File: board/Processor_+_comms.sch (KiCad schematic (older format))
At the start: 39 parts, among them U11 ATXMEGA256A3U-MH, U12 NTS0104, U14 TC1015-3.3VCT713

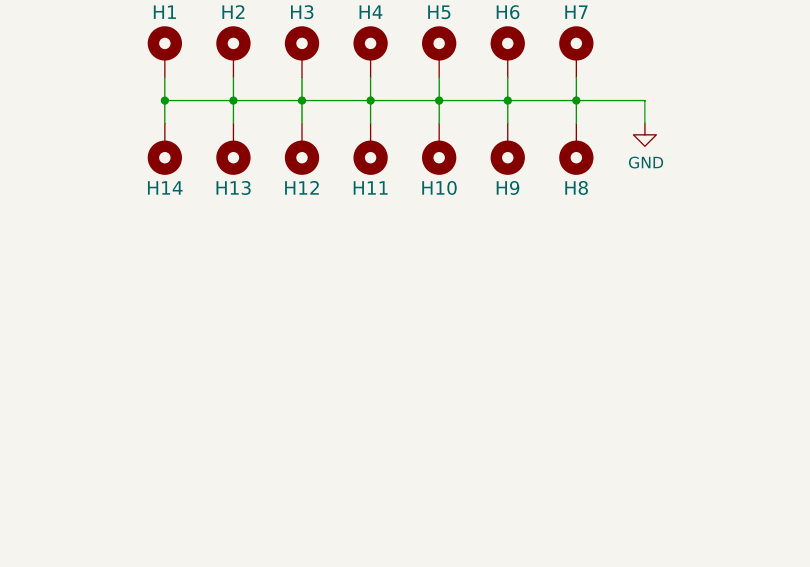
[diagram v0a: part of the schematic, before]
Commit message: Added two fiducial marks and fixed a couple more footprints
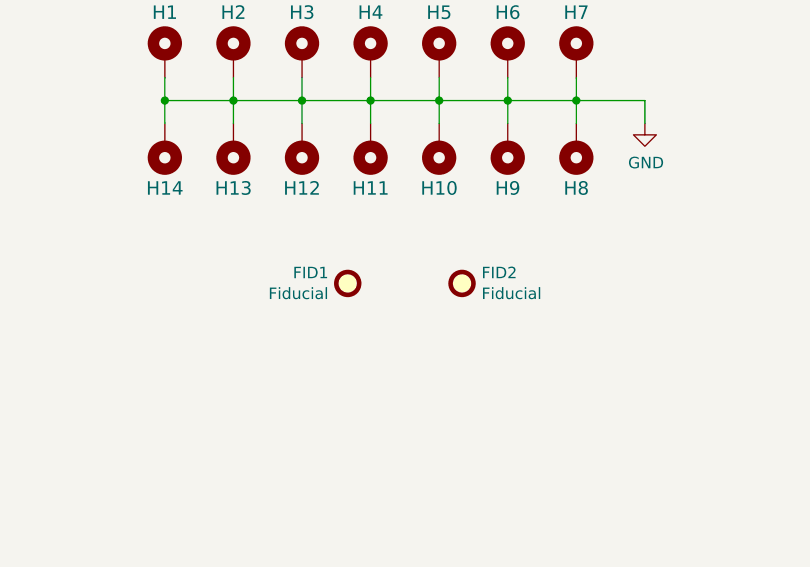
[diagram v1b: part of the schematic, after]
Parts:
- added FID1, FID2: Fiducial, Fiducial:Fiducial_1mm_Mask2mm, symbol Mechanical:Fiducial
- OSC1: footprint MXKeyboard_RGB:7M -> rhais_osc:SMD3225
- U12: footprint MXKeyboard_RGB:DHVQFN-14 -> rhais_package-qfn:DHVQFN-14-1EP_2.5x3mm_P0.5mm_EP1x1.5mm
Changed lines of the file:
@@
 F 0 "U12" H 13200 5980 59  0000 R TNN
 F 1 "NTS0104" H 12400 5980 59  0000 L TNN
-F 2 "MXKeyboard_RGB:DHVQFN-14" H 12800 6500 50  0001 C CNN
+F 2 "rhais_package-qfn:DHVQFN-14-1EP_2.5x3mm_P0.5mm_EP1x1.5mm" H 12800 6500 50  0001 C CNN
 F 3 "" H 12800 6500 50  0001 C CNN
 F 4 "NXP" H 12800 6500 59  0001 L BNN "MFR"
@@
 F 0 "OSC1" H 10000 1780 85  0000 L TNN
 F 1 "16MHz" H 9500 2620 85  0000 L BNN
-F 2 "MXKeyboard_RGB:7M" H 9900 2200 50  0001 C CNN
+F 2 "rhais_osc:SMD3225" H 9900 2200 50  0001 C CNN
 F 3 "" H 9900 2200 50  0001 C CNN
 F 4 "Multicomp" H 9900 2200 85  0001 L BNN "ALT_MFR"
@@
 $EndComp
 NoConn ~ 3900 2300
+$Comp
+L Mechanical:Fiducial FID1
+U 1 1 603C2F69
+P 13000 3000
+F 0 "FID1" H 12916 2954 50  0000 R CNN
+F 1 "Fiducial" H 12916 3045 50  0000 R CNN
+F 2 "Fiducial:Fiducial_1mm_Mask2mm" H 13000 3000 50  0001 C CNN
+F 3 "~" H 13000 3000 50  0001 C CNN
+	1    13000 3000
+	1    0    0    1
+$EndComp
+$Comp
+L Mechanical:Fiducial FID2
+U 1 1 603C34BD
+P 13500 3000
+F 0 "FID2" H 13585 3046 50  0000 L CNN
+F 1 "Fiducial" H 13585 2955 50  0000 L CNN
+F 2 "Fiducial:Fiducial_1mm_Mask2mm" H 13500 3000 50  0001 C CNN
+F 3 "~" H 13500 3000 50  0001 C CNN
+	1    13500 3000
+	1    0    0    -1
+$EndComp
 Wire Bus Line
 	4350 4400 4350 4800

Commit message: Renamed MXKeyboard_RGB => MXKeyboard and cleaned up the last of the old Eagle files we aren't using now
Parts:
- OSC1: symbol MXKeyboard_RGB-eagle-import:CXO-7M -> MXKeyboard-eagle-import:CXO-7M
- PS/2: footprint MXKeyboard_RGB:TM_0508_A_6 -> MXKeyboard:TM_0508_A_6; symbol MXKeyboard_RGB-eagle-import:PS_2 -> MXKeyboard-eagle-import:PS_2
- U11: symbol MXKeyboard_RGB-eagle-import:ATXMEGA256A3U-MH -> MXKeyboard-eagle-import:ATXMEGA256A3U-MH
- U12: symbol MXKeyboard_RGB-eagle-import:NTS0104 -> MXKeyboard-eagle-import:NTS0104
- U14: symbol MXKeyboard_RGB-eagle-import:TC1015-3.3VCT713 -> MXKeyboard-eagle-import:TC1015-3.3VCT713
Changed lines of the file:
@@
 $EndComp
 $Comp
-L MXKeyboard_RGB-eagle-import:PS_2 PS/2
+L MXKeyboard-eagle-import:PS_2 PS/2
 U 1 1 554878EE
 P 14300 6300
@@
 F 0 "PS/2" H 14300 6300 50  0001 C CNN
 F 1 "PS_2" H 14300 6300 50  0001 C CNN
-F 2 "MXKeyboard_RGB:TM_0508_A_6" H 14300 6300 50  0001 C CNN
+F 2 "MXKeyboard:TM_0508_A_6" H 14300 6300 50  0001 C CNN
 F 3 "https://downloads.lumberg.com/datenblaetter/en/tm0508a.pdf" H 14300 6300 50  0001 C CNN
 F 4 "https://uk.farnell.com/lumberg/tm-0508-a-6/socket-mini-din-chassis-6-way/dp/1200113" H 14300 6300 50  0001 C CNN "URL_FARNELL"
@@
 $EndComp
 $Comp
-L MXKeyboard_RGB-eagle-import:NTS0104 U12
+L MXKeyboard-eagle-import:NTS0104 U12
 U 1 1 A9F22F29
 P 12800 6500
@@
 $EndComp
 $Comp
-L MXKeyboard_RGB-eagle-import:TC1015-3.3VCT713 U14
+L MXKeyboard-eagle-import:TC1015-3.3VCT713 U14
 U 1 1 9D30ECAF
 P 7700 2200
@@
 $EndComp
 $Comp
-L MXKeyboard_RGB-eagle-import:CXO-7M OSC1
+L MXKeyboard-eagle-import:CXO-7M OSC1
 U 1 1 01133300
 P 9900 2200
@@
 $EndComp
 $Comp
-L MXKeyboard_RGB-eagle-import:ATXMEGA256A3U-MH U11
+L MXKeyboard-eagle-import:ATXMEGA256A3U-MH U11
 U 1 1 43CCD586
 P 5700 5800

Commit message: Cleaned up the BOM and added all the missing BOM information I could find
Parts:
- C1, C2, C3, C4, C5, C6, C7, C8, C9: URL_FARNELL (none) -> https://uk.farnell.com/multicomp/mc0603b104j250ct/cap-0-1-f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
- C11, C13: MPN MC0603X105K100CT -> MC0603B105K160CT; OC_FARNELL 1759399 -> 2320814; URL_FARNELL https://uk.farnell.com/multicomp/mc0603x105k100ct/cap-1-f-1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 -> https://uk.farnell.com/multicomp/mc0603b105k160ct/cap-1-f-1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
- JP1: MFR (none) -> Amphenol ICC; MPN (none) -> 20021121-00010C4LF; OC_FARNELL (none) -> 1865279; URL_FARNELL (none) -> https://uk.farnell.com/amphenol-icc-fci/20021121-00010c4lf/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
- OSC1: ALT_MFR Multicomp -> (none); ALT_MPN MCSJK-3N-16.00-3.3-25-B -> (none); ALT_OC_FARNELL 2854286 -> (none); ALT_URL https://uk.farnell.com/multicomp/mcsjk-3n-16-00-3-3-25-b/os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 -> (none); MFR IQD -> Multicomp; MPN LFSPXO025494 -> MCSJK-3N-16.00-3.3-25-B; OC_FARNELL 2449455 -> 2854286; URL_FARNELL http://uk.farnell.com/iqd-frequency-products/lfspxo025494/o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 -> https://uk.farnell.com/multicomp/mcsjk-3n-16-00-3-3-25-b/os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
- R17, R19: MFR Vishay -> Multicomp; MPN CRCW08051M00FKEA -> MCWR06X1004FTL; OC_FARNELL 1652946 -> 2447285; URL_FARNELL https://uk.farnell.com/vishay/crcw08051m00fkea/res-1m-1-0-1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 -> https://uk.farnell.com/multicomp/mcwr06x1004ftl/res-1m-1-0-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
- R18, R38: MPN MC0063W0603110K -> MCWR06X1002FTL; OC_FARNELL 2130939 -> 2446547; URL_FARNELL (none) -> https://uk.farnell.com/multicomp/mcwr06x1002ftl/res-10k-1-0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
- R37: MFR (none) -> Multicomp; MPN (none) -> MCWR06X1003FTL; OC_FARNELL (none) -> 2447226; URL_FARNELL (none) -> https://uk.farnell.com/multicomp/mcwr06x1003ftl/res-100k-1-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
- U11: MFR (none) -> Atmel; MPN (none) -> ATXMEGA256A3U-MH; OC_FARNELL (none) -> 2066308; URL_FARNELL (none) -> https://uk.farnell.com/microchip/atxmega256a3u-mh/mcu-8bit-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
- U14: MFR (none) -> Microchip; MPN (none) -> TC1015-3.3VCT713; OC_FARNELL (none) -> 1331505; URL_FARNELL (none) -> https://uk.farnell.com/microchip/tc1015-3-3vct713/ic-v-reg-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
- USB: MFR (none) -> Amphenol ICC; MPN (none) -> 10103593-0001LF; OC_FARNELL (none) -> 2293751; URL_FARNELL (none) -> https://uk.farnell.com/amphenol-icc-fci/10103593-0001lf/mic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

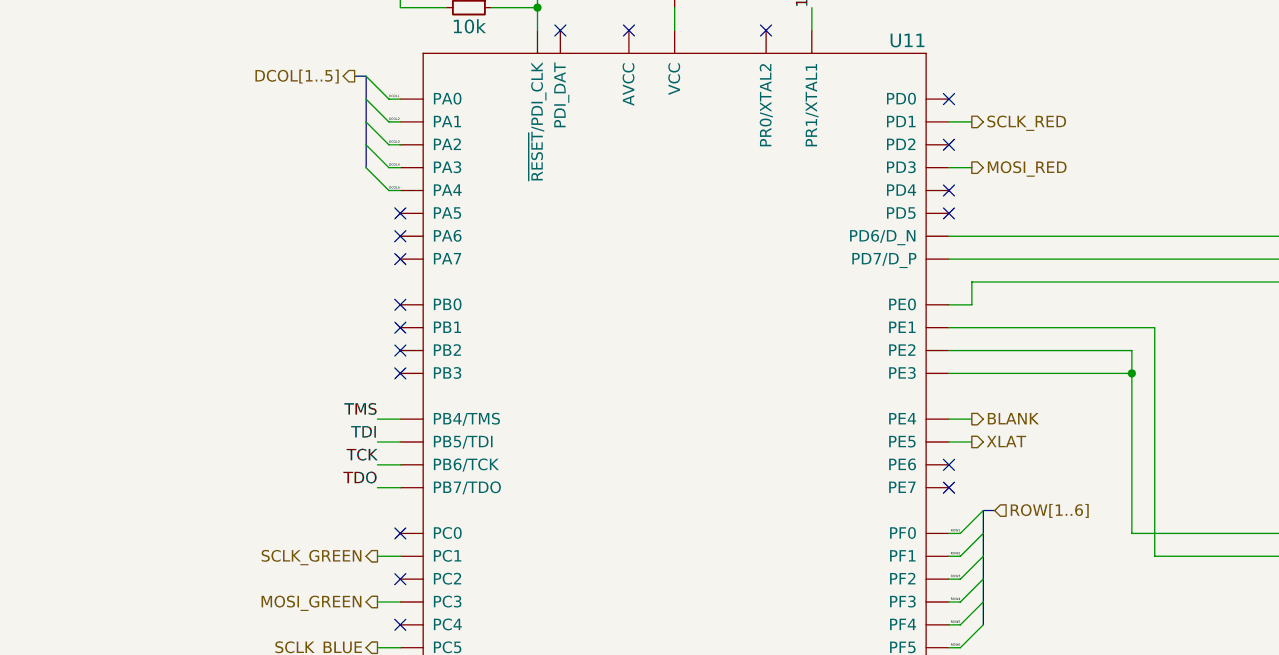
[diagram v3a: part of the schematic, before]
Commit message: Added a Molex PicoBlade based debug connector to the board
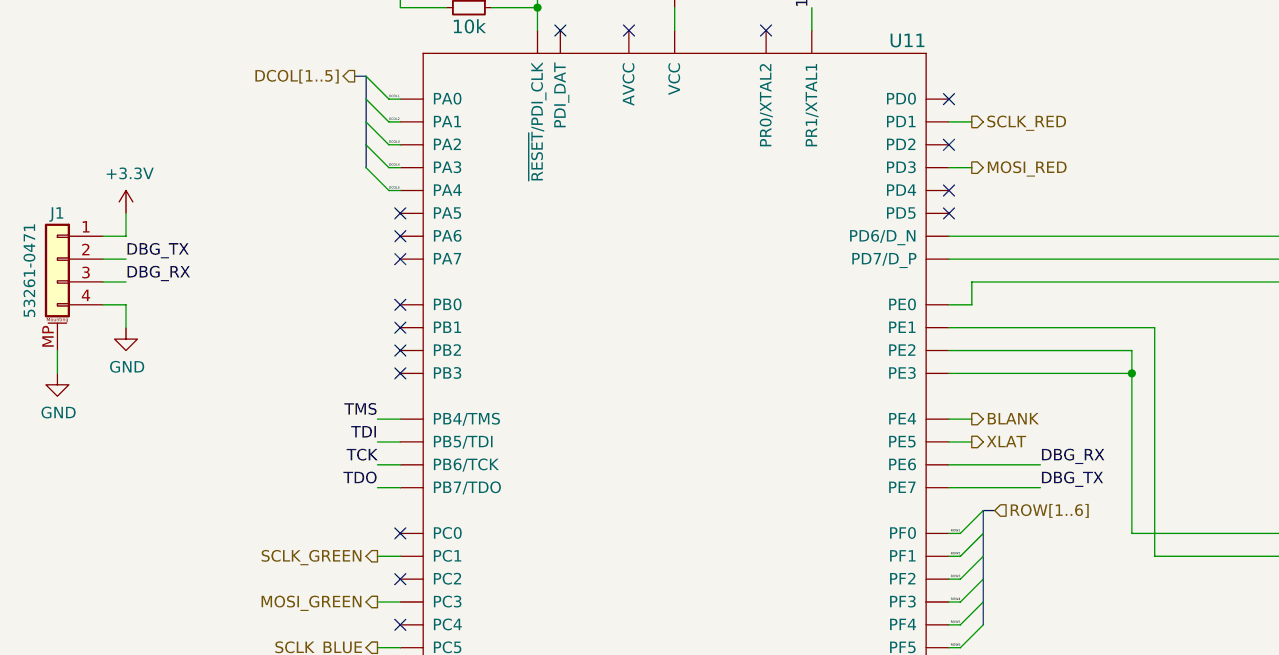
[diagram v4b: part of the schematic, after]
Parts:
- added J1: 53261-0471, rhais_connector-molex:Molex_PicoBlade_53261-0471_1x04-1MP_P1.25mm_Horizontal, symbol Connector_Generic_MountingPin:Conn_01x04_MountingPin
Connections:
- net +3V3: now also J1.1 (Pin_1)
- net GND: now also J1.4 (Pin_4), J1.MP (MountPin)
- net DBG_RX: now reaches U11.42 (PE6)
- net DBG_RX: now also J1.3 (Pin_3)
- net DBG_TX: now reaches U11.43 (PE7)
- net DBG_TX: now also J1.2 (Pin_2)
- no-connect marks 29 -> 27
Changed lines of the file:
@@
 NoConn ~ 6900 7100
 NoConn ~ 6900 7000
-NoConn ~ 6900 6200
-NoConn ~ 6900 6100
 NoConn ~ 4500 7000
 NoConn ~ 4500 6800
@@
 	1    0    0    -1
 $EndComp
+$Comp
+L Connector_Generic_MountingPin:Conn_01x04_MountingPin J1
+U 1 1 5FC1037E
+P 3000 5200
+F 0 "J1" H 3000 5400 50  0000 C CNN
+F 1 "53261-0471" V 3150 5150 50  0000 C BNN
+F 2 "rhais_connector-molex:Molex_PicoBlade_53261-0471_1x04-1MP_P1.25mm_Horizontal" H 3000 5200 50  0001 C CNN
+F 3 "https://www.molex.com/webdocs/datasheets/pdf/en-us/0532610471_PCB_HEADERS.pdf" H 3000 5200 50  0001 C CNN
+F 4 "53261-0471" H 3000 5200 50  0001 C CNN "MPN"
+F 5 "Molex" H 3000 5200 50  0001 C CNN "MFR"
+F 6 "1125374" H 3000 5200 50  0001 C CNN "OC_FARNELL"
+F 7 "https://uk.farnell.com/molex/53261-0471/connector-header-4pos-1row-1-25mm/dp/1125374" H 3000 5200 50  0001 C CNN "URL_FARNELL"
+	1    3000 5200
+	-1   0    0    -1
+$EndComp
+$Comp
+L power:GND #PWR071
+U 1 1 5FC1118A
+P 3000 5700
+F 0 "#PWR071" H 3000 5450 50  0001 C CNN
+F 1 "GND" H 3005 5527 50  0000 C CNN
+F 2 "" H 3000 5700 50  0001 C CNN
+F 3 "" H 3000 5700 50  0001 C CNN
+	1    3000 5700
+	1    0    0    -1
+$EndComp
+Wire Wire Line
+	3000 5600 3000 5700
+Wire Wire Line
+	6900 6100 7300 6100
+Wire Wire Line
+	6900 6200 7300 6200
+Text Label 7300 6200 0    50   ~ 0
+DBG_TX
+Text Label 7300 6100 0    50   ~ 0
+DBG_RX
+$Comp
+L power:GND #PWR0102
+U 1 1 5FC88EB6
+P 3300 5500
+F 0 "#PWR0102" H 3300 5250 50  0001 C CNN
+F 1 "GND" H 3305 5327 50  0000 C CNN
+F 2 "" H 3300 5500 50  0001 C CNN
+F 3 "" H 3300 5500 50  0001 C CNN
+	1    3300 5500
+	1    0    0    -1
+$EndComp
+$Comp
+L power:+3.3V #PWR0103
+U 1 1 5FC891F5
+P 3300 5000
+F 0 "#PWR0103" H 3300 4850 50  0001 C CNN
+F 1 "+3.3V" H 3315 5173 50  0000 C CNN
+F 2 "" H 3300 5000 50  0001 C CNN
+F 3 "" H 3300 5000 50  0001 C CNN
+	1    3300 5000
+	1    0    0    -1
+$EndComp
+Wire Wire Line
+	3200 5100 3300 5100
+Wire Wire Line
+	3300 5100 3300 5000
+Wire Wire Line
+	3200 5400 3300 5400
+Wire Wire Line
+	3300 5400 3300 5500
+Wire Wire Line
+	3200 5200 3300 5200
+Wire Wire Line
+	3200 5300 3300 5300
 Wire Bus Line
 	4350 4400 4350 4800
 Wire Bus Line
 	7050 6300 7050 6800
+Text Label 3300 5200 0    50   ~ 0
+DBG_TX
+Text Label 3300 5300 0    50   ~ 0
+DBG_RX
 $EndSCHEMATC

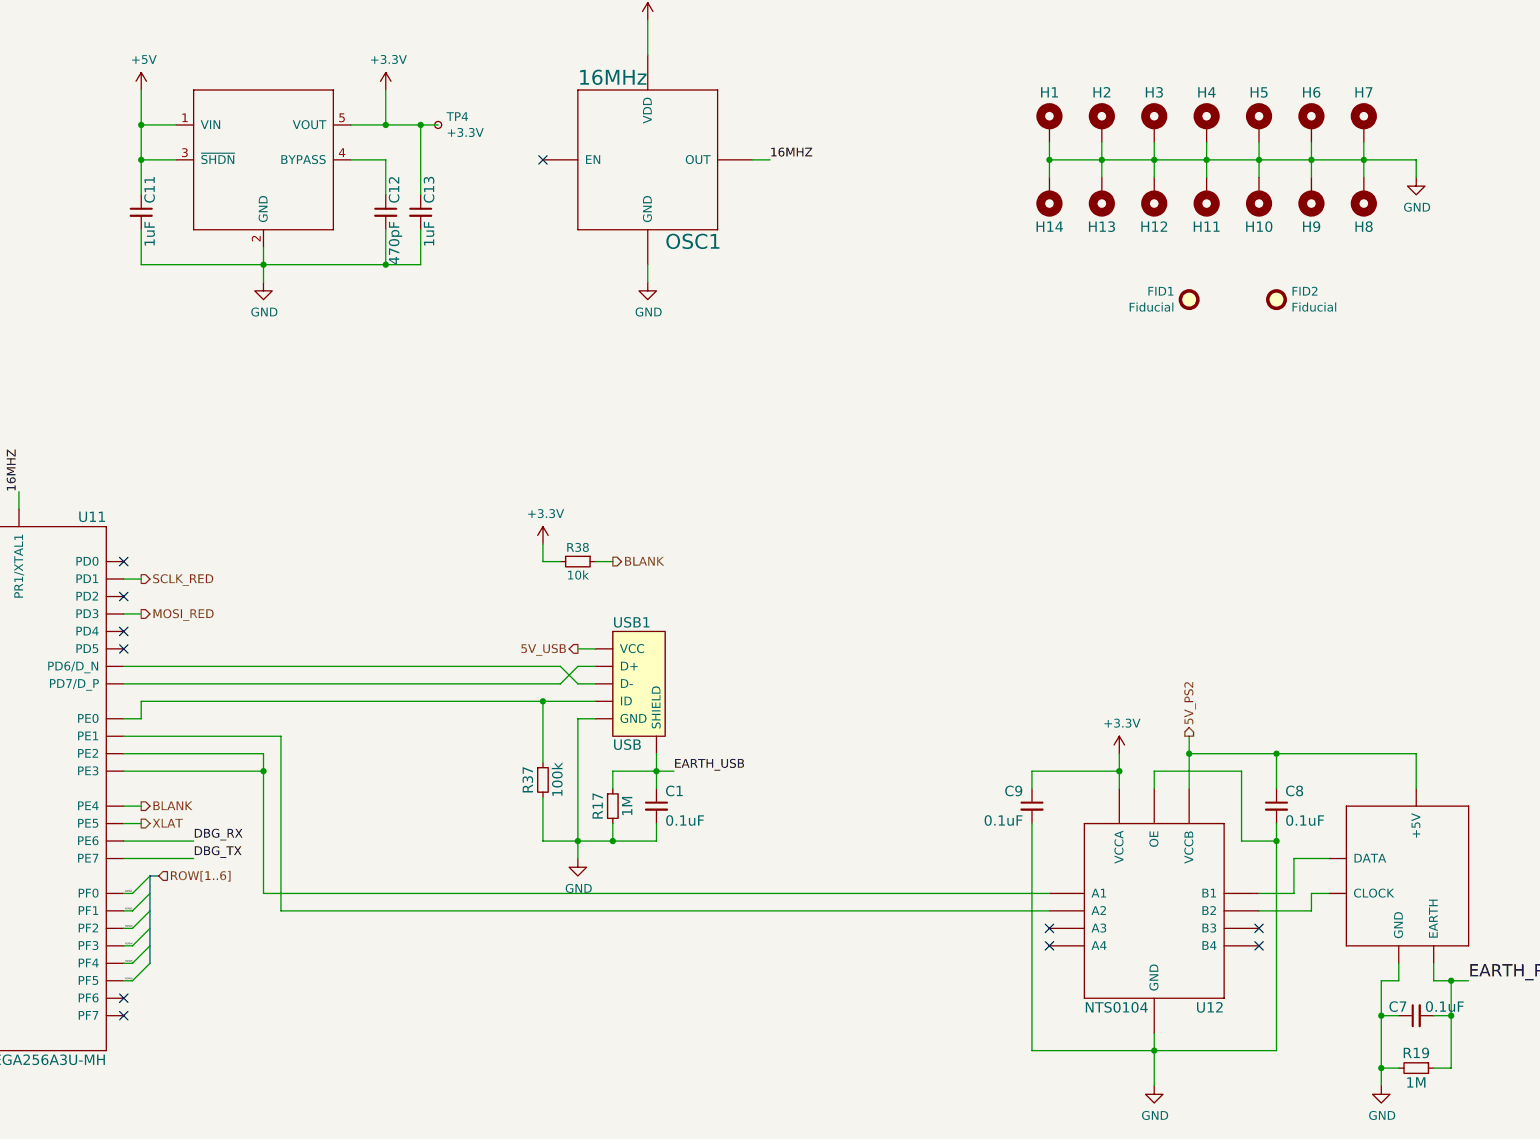
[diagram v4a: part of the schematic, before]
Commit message: Replaced the USB port with a 2.0 mode Type-C connector
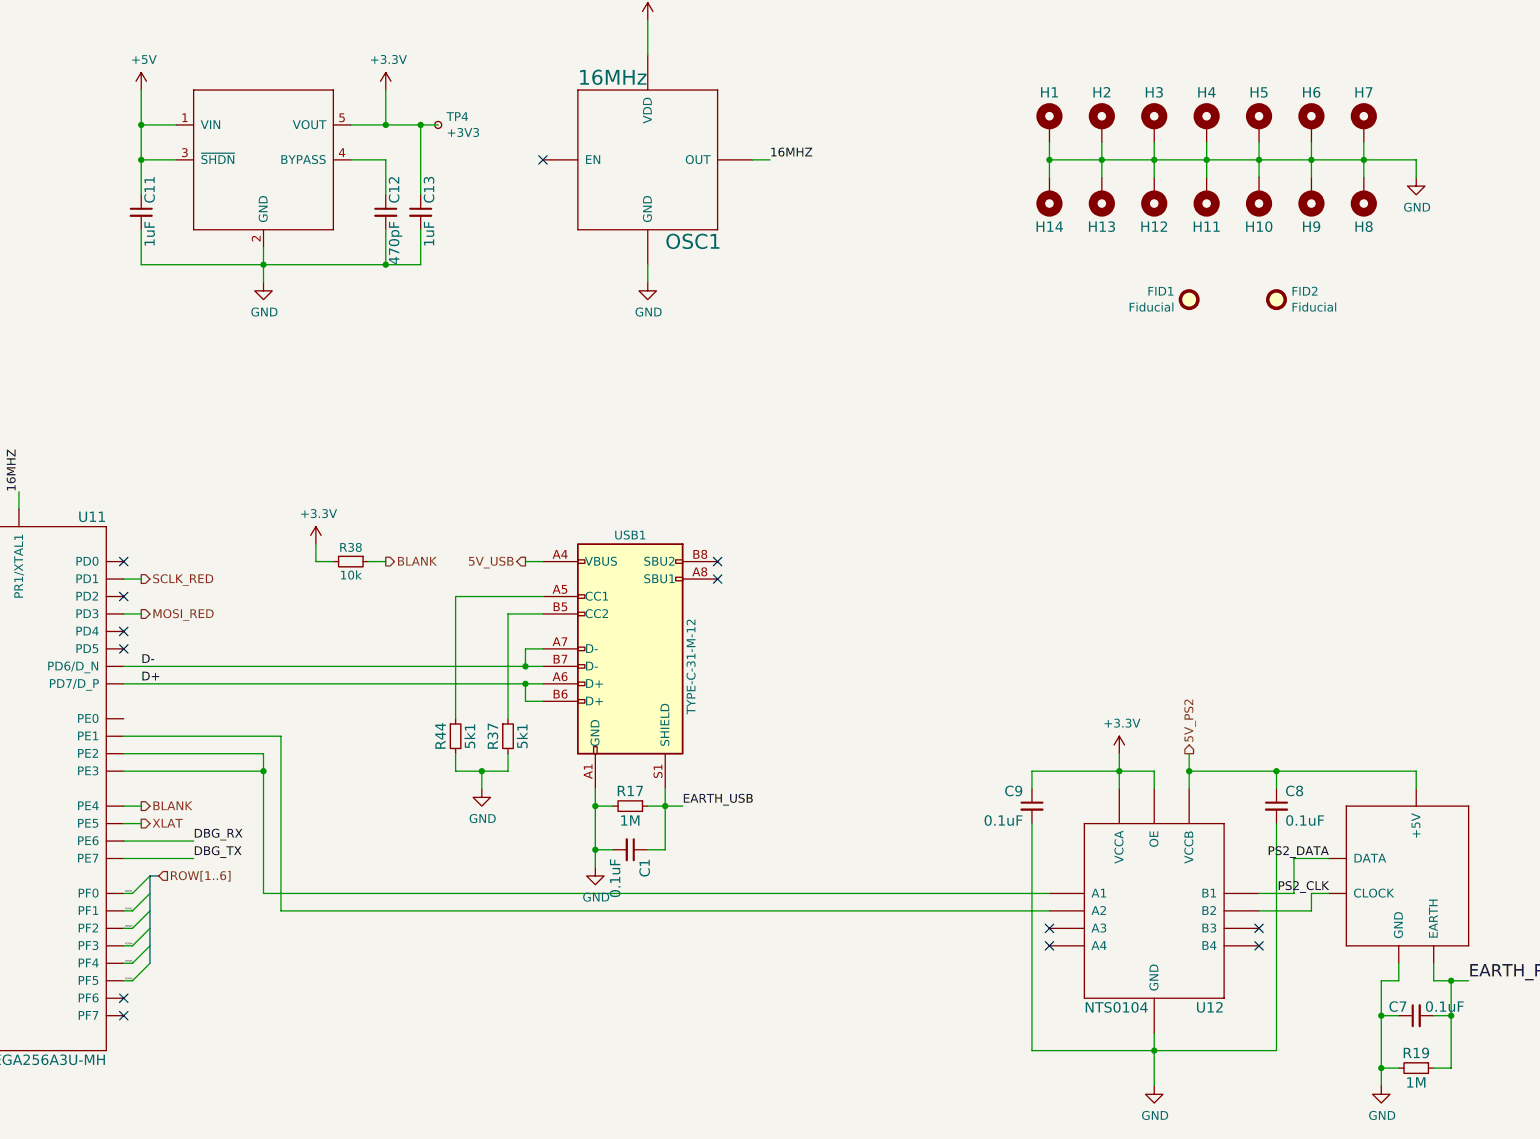
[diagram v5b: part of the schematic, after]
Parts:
- removed USB: USB, rhais_usb:MICRO-USB-B-(IN_PCB), symbol DX_MON:USB-Micro-B
- added R44: 5k1, rhais_rcl:R0603, symbol Device:R_Small
- added USB1: TYPE-C-31-M-12, rhais_usb:USB_C_Receptacle_HRO_TYPE-C-31-M-12, symbol DX_MON:USB_C_Receptacle_USB2.0
- R37: value 100k -> 5k1
- TP4: value +3.3V -> +3V3
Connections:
- net +3V3: now also U12.8 (OE)
- net 5V_USB: now also USB1.A4 (VBUS), USB1.A9 (VBUS), USB1.B4 (VBUS), USB1.B9 (VBUS)
- net EARTH_USB: now also USB1.S1 (SHIELD)
- net GND: now also R44.2, USB1.A1 (GND), USB1.A12 (GND), USB1.B1 (GND), USB1.B12 (GND); no longer U12.8 (OE)
- net D-: now reaches U11.32 (PD6/D_N)
- net D-: now also USB1.A7 (D-), USB1.B7 (D-)
- net D+: now reaches U11.33 (PD7/D_P)
- net D+: now also USB1.A6 (D+), USB1.B6 (D+)
- net at U11.36 (PE0): no longer R37.1
- net PS2_DATA: now reaches PS/2.1 (DATA), U12.13 (B1)
- net PS2_CLK: now reaches PS/2.5 (CLOCK), U12.12 (B2)
- new net: R44.1, USB1.A5 (CC1)
- new net: R37.1, USB1.B5 (CC2)
- no-connect marks 27 -> 29
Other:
- moved on the sheet: C1, R17, R37, R38
